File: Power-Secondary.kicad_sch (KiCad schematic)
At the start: 14 parts, among them J1 PowerConn, J2 PowerConn, J3 PowerConn, Q3 SQJQ140E-T1_GE3, Q4 SQJQ140E-T1_GE3, Q5 SQJQ140E-T1_GE3, Q6 SQJQ140E-T1_GE3

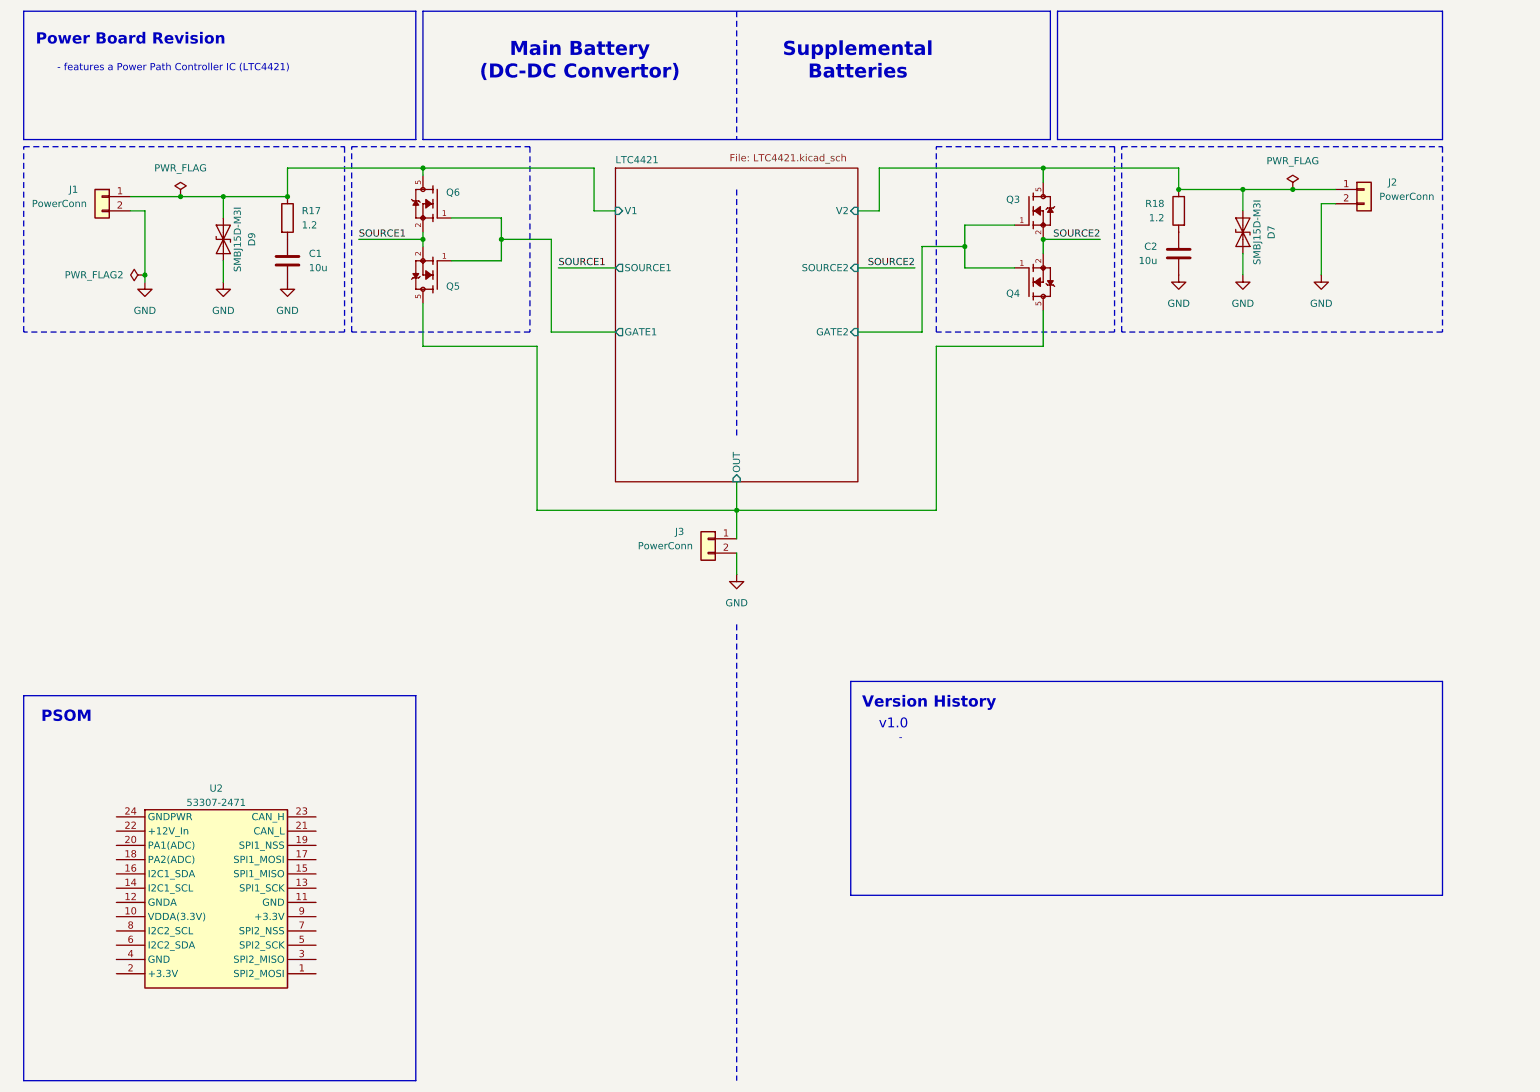
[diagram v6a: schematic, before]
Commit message: Pull up and Pull down configs for VALID, DISABLE, SHDN, RETRY
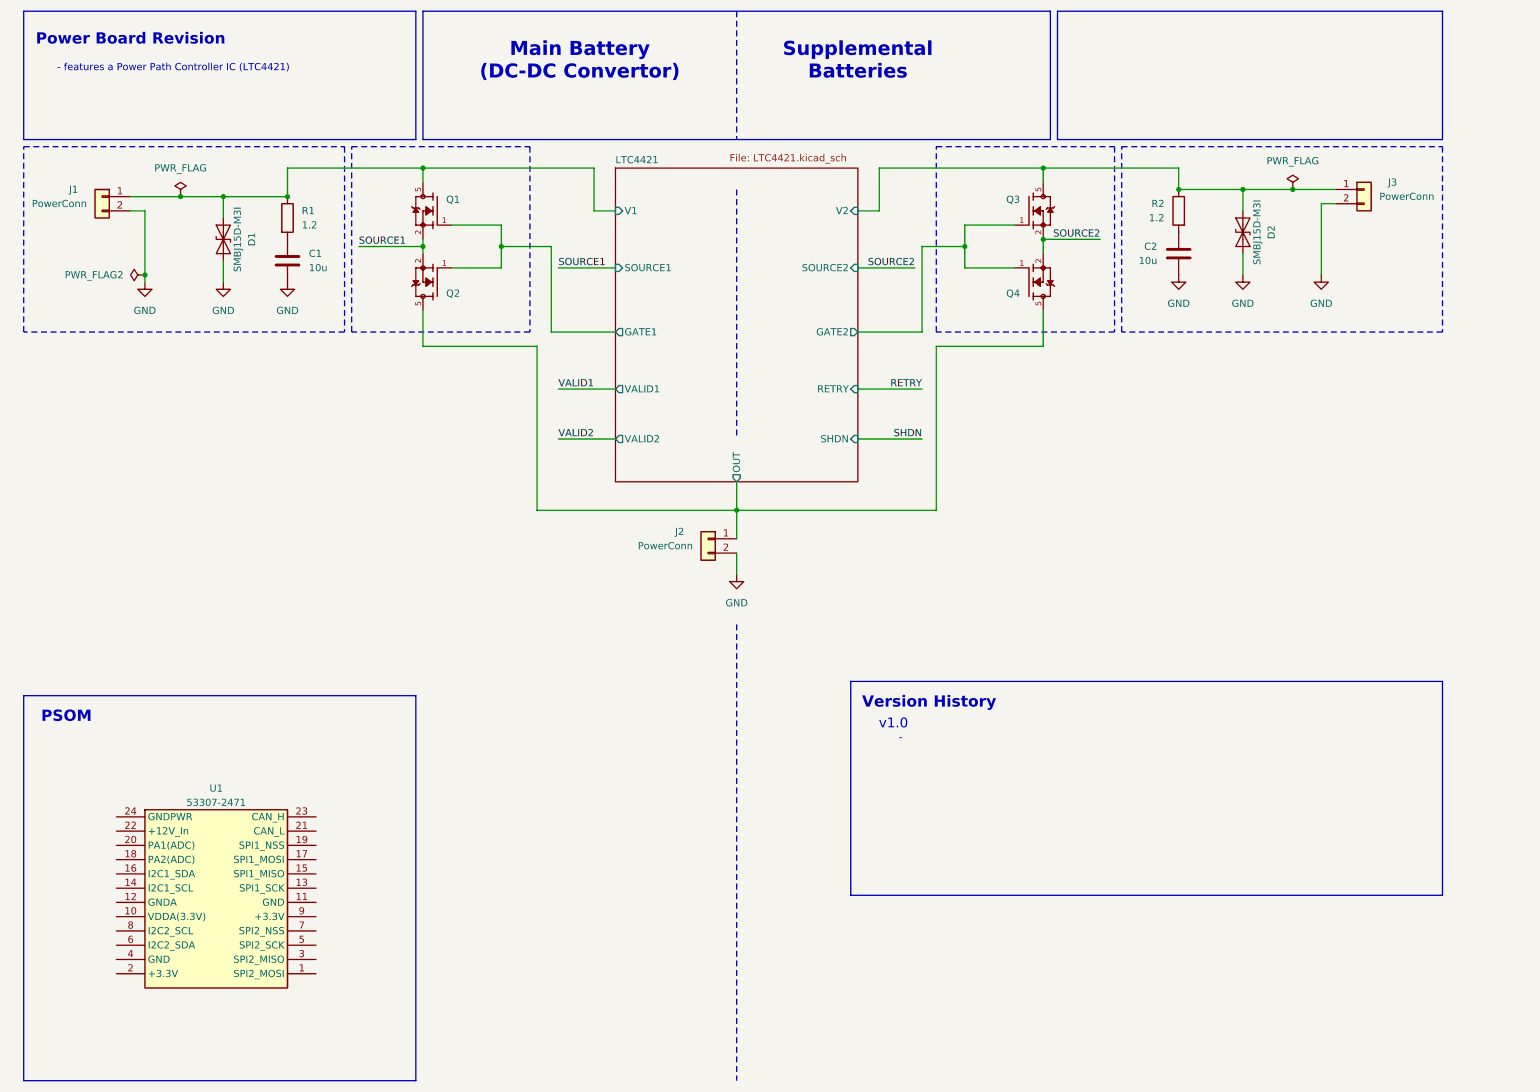
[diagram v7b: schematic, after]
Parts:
- renumbered D9 to D1, D7 to D2, J3 to J2, J2 to J3, Q6 to Q1, Q5 to Q2, R17 to R1, R18 to R2, U2 to U1
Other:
- sheet LTC4421 ports: added RETRY, SHDN, VALID1, VALID2; removed none
- moved on the sheet: Q1, Q2

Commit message: small changes
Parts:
- U1: value ~ -> PeripheralSOM
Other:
- moved on the sheet: C2, D2, J3, Q3, Q4, R2
